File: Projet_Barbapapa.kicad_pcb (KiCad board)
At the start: 2 copper layers, 85.1 x 99.9 mm, 47 parts, among them J1 USB_C_Receptacle_USB2.0, J2 Speaker, J3 Conn_01x02, J4 LCD SPI, J5 LCD Soft SPI, J6 Random FTDI, J7 NFC1, J8 NFC2, J9 RGB_LED, SW2 Power switch, U1 MAX98357A/B, U2 AP61201Z6-7 buck, U3 MAX1811, U4 CD4051B

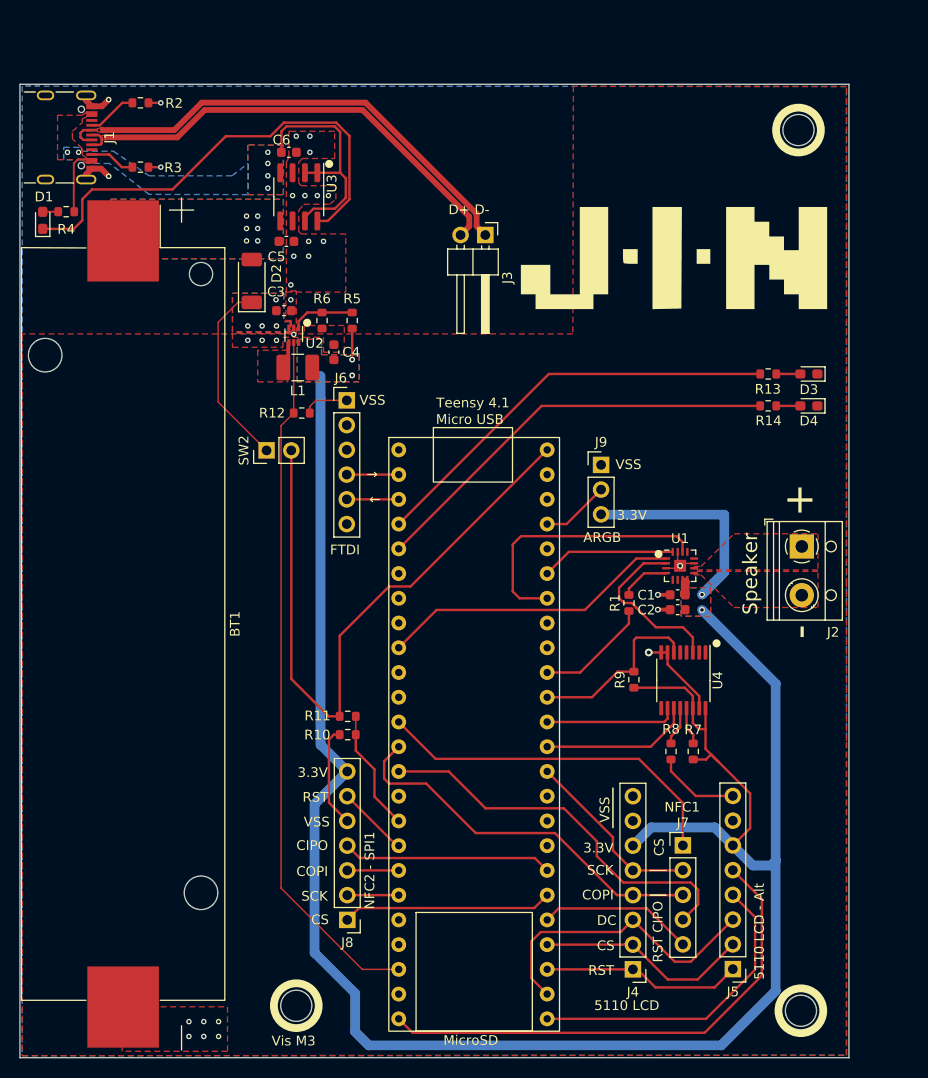
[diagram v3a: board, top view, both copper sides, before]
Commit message: Corrections et expansion de masque
Quelques ajustements de routage au cas où, pour VIN et une branche thermique
sur VSS.
Ajustement de la marge sur le plan de masse du dessus (plus grande).
Vérification de l'expansion de masque pour le passage à 2 couches.
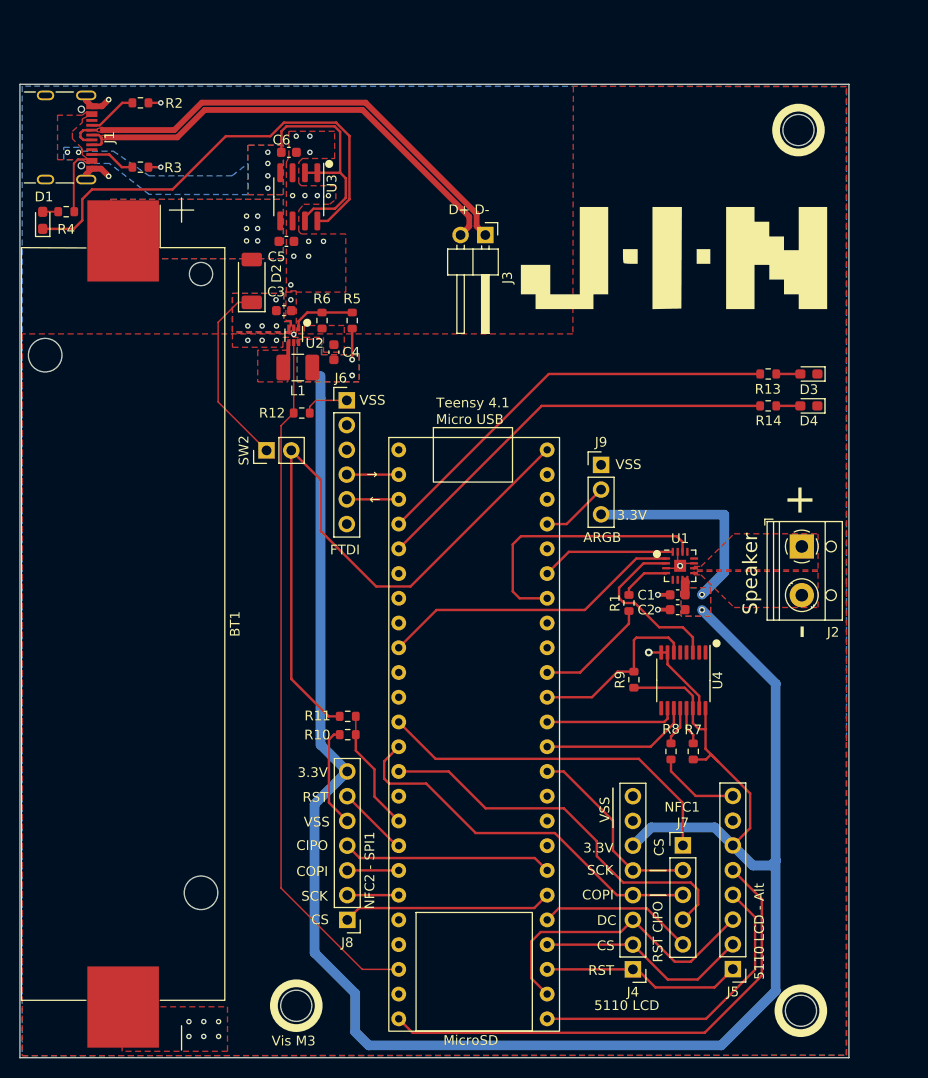
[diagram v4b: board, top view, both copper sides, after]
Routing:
- net /Power and USB/VIN: track 67.5 -> 71.0 mm
- net /SPI_SCK: track 18.9 -> 19.9 mm
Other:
- rule pad_to_mask_clearance: 0 -> 0.038
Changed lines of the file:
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@@
       (dielectric_constraints no)
     )
-    (pad_to_mask_clearance 0)
+    (pad_to_mask_clearance 0.038)
     (pcbplotparams
       (layerselection 0x00010fc_ffffffff)
@@
     (effects (font (size 0.8 0.8) (thickness 0.153)) (justify left bottom))
   )
-  (gr_text "●" (at 82.6902 110.7134) (layer "F.SilkS")
+  (gr_text "●" (at 82.5246 110.7134) (layer "F.SilkS")
     (effects (font (size 0.8 0.8) (thickness 0.153)) (justify left bottom))
   )
@@
   (segment (start 78.9001 145.359) (end 72.5247 138.9836) (width 0.25) (layer "F.Cu") (net 17))
   (segment (start 72.5247 138.9836) (end 64.3967 138.9836) (width 0.25) (layer "F.Cu") (net 17))
-  (segment (start 78.486 139.4127) (end 71.7323 132.659) (width 0.25) (layer "F.Cu") (net 18))
+  (segment (start 78.486 137.7188) (end 73.4262 132.659) (width 0.25) (layer "F.Cu") (net 18))
+  (segment (start 78.486 140.7688) (end 78.486 137.7188) (width 0.25) (layer "F.Cu") (net 18))
   (segment (start 85.6416 142.819) (end 85.667 142.7936) (width 0.25) (layer "F.Cu") (net 18))
-  (segment (start 80.5362 142.819) (end 78.486 140.7688) (width 0.25) (layer "F.Cu") (net 18))
   (segment (start 80.5362 142.819) (end 85.6416 142.819) (width 0.25) (layer "F.Cu") (net 18))
-  (segment (start 78.486 140.7688) (end 78.486 139.4127) (width 0.25) (layer "F.Cu") (net 18))
+  (segment (start 73.4262 132.659) (end 71.7323 132.659) (width 0.25) (layer "F.Cu") (net 18))
+  (segment (start 80.5362 142.819) (end 78.486 140.7688) (width 0.25) (layer "F.Cu") (net 18))
   (segment (start 88.0424 158.059) (end 93.0838 153.0176) (width 0.25) (layer "F.Cu") (net 19))
   (segment (start 93.0838 153.0176) (end 93.0838 147.6196) (width 0.25) (layer "F.Cu") (net 19))
@@
   (segment (start 84.1938 118.9176) (end 84.7428 119.4666) (width 0.25) (layer "F.Cu") (net 39))
   (segment (start 84.7428 119.4666) (end 84.7428 120.4416) (width 0.25) (layer "F.Cu") (net 39))
-  (segment (start 57.7063 113.665) (end 55.499 113.665) (width 0.25) (layer "F.Cu") (net 40))
+  (segment (start 57.7063 113.665) (end 54.1782 113.665) (width 0.25) (layer "F.Cu") (net 40))
+  (segment (start 48.4886 107.9754) (end 48.4886 102.7226) (width 0.25) (layer "F.Cu") (net 40))
   (segment (start 45.461 123.1596) (end 49.3014 127) (width 0.25) (layer "F.Cu") (net 40))
-  (segment (start 45.461 99.695) (end 45.461 123.1596) (width 0.25) (layer "F.Cu") (net 40))
   (segment (start 71.7323 99.639) (end 57.7063 113.665) (width 0.25) (layer "F.Cu") (net 40))
-  (segment (start 50.4322 118.7318) (end 50.4322 127) (width 0.25) (layer "F.Cu") (net 40))
+  (segment (start 45.461 99.695) (end 45.461 123.1596) (width 0.25) (layer "F.Cu") (net 40))
+  (segment (start 54.1782 113.665) (end 48.4886 107.9754) (width 0.25) (layer "F.Cu") (net 40))
   (segment (start 49.3014 127) (end 50.4322 127) (width 0.25) (layer "F.Cu") (net 40))
-  (segment (start 55.499 113.665) (end 50.4322 118.7318) (width 0.25) (layer "F.Cu") (net 40))
+  (segment (start 48.4886 102.7226) (end 45.461 99.695) (width 0.25) (layer "F.Cu") (net 40))
   (segment (start 60.3733 116.078) (end 75.6034 116.078) (width 0.25) (layer "F.Cu") (net 44))
   (segment (start 75.6034 116.078) (end 80.8875 110.7939) (width 0.25) (layer "F.Cu") (net 44))
@@
   (segment (start 73.9649 110.1064) (end 84.6316 110.1064) (width 0.25) (layer "F.Cu") (net 52))
   (segment (start 71.7323 112.339) (end 73.9649 110.1064) (width 0.25) (layer "F.Cu") (net 52))
-  (segment (start 85.6672 117.856) (end 82.8986 117.856) (width 0.25) (layer "F.Cu") (net 59))
-  (segment (start 81.6191 111.2939) (end 83.9441 111.2939) (width 0.25) (layer "F.Cu") (net 59))
-  (segment (start 79.6218 115.3616) (end 79.1138 114.8536) (width 0.25) (layer "F.Cu") (net 59))
-  (segment (start 79.1138 114.8536) (end 79.1138 113.7992) (width 0.25) (layer "F.Cu") (net 59))
-  (segment (start 79.1138 113.7992) (end 81.6191 111.2939) (width 0.25) (layer "F.Cu") (net 59))
-  (segment (start 80.8568 115.799375) (end 80.419025 115.3616) (width 0.25) (layer "F.Cu") (net 59))
-  (segment (start 82.8986 117.856) (end 80.8568 115.8142) (width 0.25) (layer "F.Cu") (net 59))
-  (segment (start 86.6928 120.4416) (end 86.6928 118.8816) (width 0.25) (layer "F.Cu") (net 59))
-  (segment (start 80.8568 115.8142) (end 80.8568 115.799375) (width 0.25) (layer "F.Cu") (net 59))
-  (segment (start 80.419025 115.3616) (end 79.6218 115.3616) (width 0.25) (layer "F.Cu") (net 59))
-  (segment (start 86.6928 118.8816) (end 85.6672 117.856) (width 0.25) (layer "F.Cu") (net 59))
+  (segment (start 85.6672 117.856) (end 86.6928 118.8816) (width 0.25) (layer "F.Cu") (net 59))
+  (segment (start 83.9441 111.2939) (end 81.6191 111.2939) (width 0.25) (layer "F.Cu") (net 59))
+  (segment (start 79.6218 115.3616) (end 80.7414 115.3616) (width 0.25) (layer "F.Cu") (net 59))
+  (segment (start 79.1138 114.8536) (end 79.6218 115.3616) (width 0.25) (layer "F.Cu") (net 59))
+  (segment (start 80.7414 115.3616) (end 83.2358 117.856) (width 0.25) (layer "F.Cu") (net 59))
+  (segment (start 86.6928 118.8816) (end 86.6928 120.4416) (width 0.25) (layer "F.Cu") (net 59))
+  (segment (start 83.2358 117.856) (end 85.6672 117.856) (width 0.25) (layer "F.Cu") (net 59))
+  (segment (start 79.1138 113.7992) (end 79.1138 114.8536) (width 0.25) (layer "F.Cu") (net 59))
+  (segment (start 81.6191 111.2939) (end 79.1138 113.7992) (width 0.25) (layer "F.Cu") (net 59))
   (segment (start 71.7323 147.899) (end 72.9073 146.724) (width 0.25) (layer "F.Cu") (net 65))
   (segment (start 72.9073 146.724) (end 81.9774 146.724) (width 0.25) (layer "F.Cu") (net 65))
@@
   )
   (zone (net 2) (net_name "VSS") (layer "F.Cu") (hatch edge 0.5)
-    (connect_pads thru_hole_only (clearance 0.15))
+    (connect_pads thru_hole_only (clearance 0.2))
     (min_thickness 0.25) (filled_areas_thickness no)
     (fill yes (thermal_gap 0.5) (thermal_bridge_width 0.5))
@@
         (xy 44.6532 73.4314)
         (xy 44.6532 68.3514)
-        (xy 40.9956 68.326)
+        (xy 40.9956 68.3514)
         (xy 40.9956 73.4314)
       )
